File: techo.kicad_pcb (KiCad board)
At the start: 2 copper layers, 24 parts, among them SW1 SW_Push, U1 ATmega32U4-AU, Y1 16MHz

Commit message: wired stuff together
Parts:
- moved C7 7.96 mm to (71.8, 56.5), turned to 270 degrees
- moved C3 2.08 mm to (70.9, 49.5)
- moved R2 0.76 mm to (64.1, 42.9)
- moved R3 0.76 mm to (61.0, 42.9)
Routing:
- net GND: track 0.00 -> 148.0 mm
- net +5V: track 0.00 -> 108.0 mm, vias 0 -> 8
- net Net-(R1-Pad2): track 0.00 -> 38.2 mm, vias 0 -> 2
- net Net-(R3-Pad1): track 0.00 -> 21.4 mm
- net ROW0: track 0.00 -> 20.5 mm
- net ROW1: track 0.00 -> 20.2 mm
- net Net-(R2-Pad1): track 0.00 -> 19.2 mm
- net COL0: track 0.00 -> 19.1 mm
- net COL1: track 0.00 -> 19.0 mm
- net Net-(C2-Pad1): track 0.00 -> 14.4 mm
- net Net-(C1-Pad1): track 0.00 -> 11.6 mm
- net VCC: track 0.00 -> 9.38 mm
- net Net-(D1-Pad2): track 0.00 -> 7.81 mm
- net Net-(D3-Pad2): track 0.00 -> 7.60 mm
- net Net-(D4-Pad2): track 0.00 -> 7.53 mm
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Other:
- net class Power added: clearance 0.2, trace_width 0.381, via_dia 0.8, via_drill 0.4

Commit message: Completed tutorial
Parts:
- moved USB1 0.07 mm to (62.9, 33.6)
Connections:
- U1 pad 27: Net-(U1-Pad27) -> ROW0
- U1 pad 28: Net-(U1-Pad28) -> COL1
- U1 pad 29: Net-(U1-Pad29) -> COL0
- U1 pad 30: Net-(U1-Pad30) -> ROW1
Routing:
- net COL1: track 19.0 -> 56.6 mm
- net ROW1: track 20.2 -> 52.2 mm
- net ROW0: track 20.5 -> 51.1 mm
- net COL0: track 19.1 -> 37.3 mm
- net +5V: track 108.0 -> 109.2 mm, vias 8 -> 9
- net VCC: track 9.38 -> 10.1 mm
- added copper zone on B.Cu, net GND

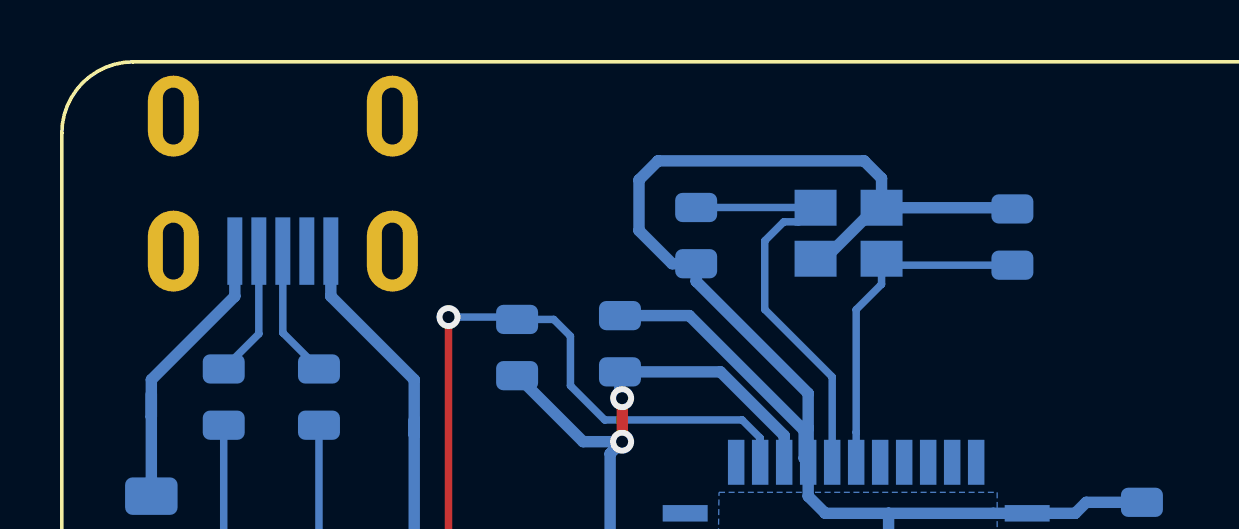
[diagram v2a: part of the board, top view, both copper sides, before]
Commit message: Started making keyboard matrix
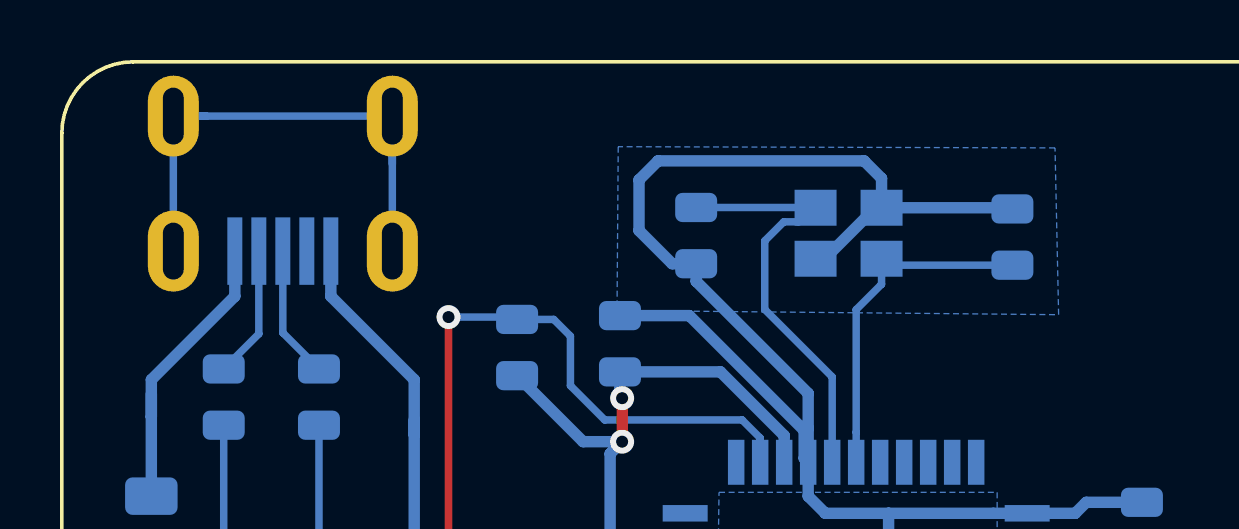
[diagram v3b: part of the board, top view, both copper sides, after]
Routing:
- net Net-(USB1-Pad6): track 0.00 -> 19.0 mm
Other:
- rule via_min_size: 0.4 -> 0.04
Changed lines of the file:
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@@
     (thickness 1.6)
     (drawings 8)
-    (tracks 229)
+    (tracks 234)
     (zones 0)
     (modules 24)
@@
     (via_size 0.8)
     (via_drill 0.4)
-    (via_min_size 0.4)
+    (via_min_size 0.04)
     (via_min_drill 0.3)
     (uvia_size 0.3)
@@
       (outputformat 1)
       (mirror false)
-      (drillshape 1)
+      (drillshape 0)
       (scaleselection 1)
-      (outputdirectory ""))
+      (outputdirectory "gerber/"))
   )
   (net 0 "")
@@
   (segment (start 89.599 54.8) (end 87.742 54.8) (width 0.25) (layer B.Cu) (net 20))
   (segment (start 89.789 54.61) (end 89.599 54.8) (width 0.25) (layer B.Cu) (net 20))
+  (segment (start 66.58 33.56) (end 66.58 35.16) (width 0.25) (layer B.Cu) (net 43))
+  (segment (start 59.28 33.56) (end 60.38 33.56) (width 0.25) (layer B.Cu) (net 43))
+  (segment (start 59.28 33.56) (end 66.58 33.56) (width 0.25) (layer B.Cu) (net 43))
+  (segment (start 66.58 33.56) (end 66.58 38.06) (width 0.25) (layer B.Cu) (net 43))
+  (segment (start 59.28 33.56) (end 59.28 38.06) (width 0.25) (layer B.Cu) (net 43))
   (zone (net 1) (net_name GND) (layer B.Cu) (hatch edge 0.508)
     (connect_pads (clearance 0.508))
@@
       )
     )
+  )
+  (zone (net 1) (net_name GND) (layer B.Cu) (hatch edge 0.508)
+    (connect_pads (clearance 0.508))
+    (min_thickness 0.254)
+    (fill yes (arc_segments 32) (thermal_gap 0.508) (thermal_bridge_width 0.508))
+    (polygon
+      (pts
+        (xy 88.67 34.62) (xy 74.11 34.58) (xy 74.07 40.04) (xy 88.79 40.18)
+      )
+    )
